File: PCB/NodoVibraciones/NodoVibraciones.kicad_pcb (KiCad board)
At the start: 2 copper layers, 62 x 33 mm, 26 parts, among them J1 batería, J2 UART, J4 MPU6050, SW2 SW_Push, U1 ESP-07, U2 module_mpu6050, U3 AMS1117-3.3

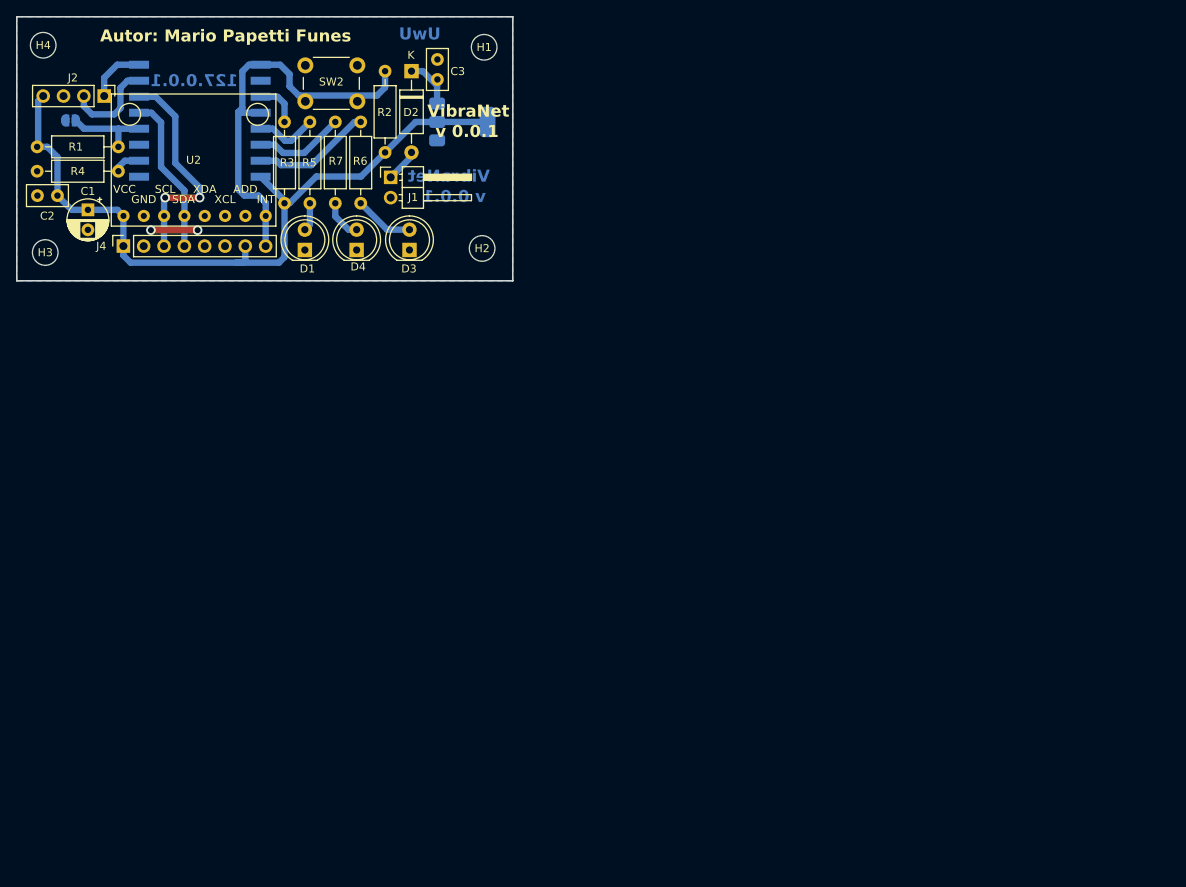
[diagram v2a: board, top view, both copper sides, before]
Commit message: Se implementaron interrupciones y diseño de PCB v1.0.8
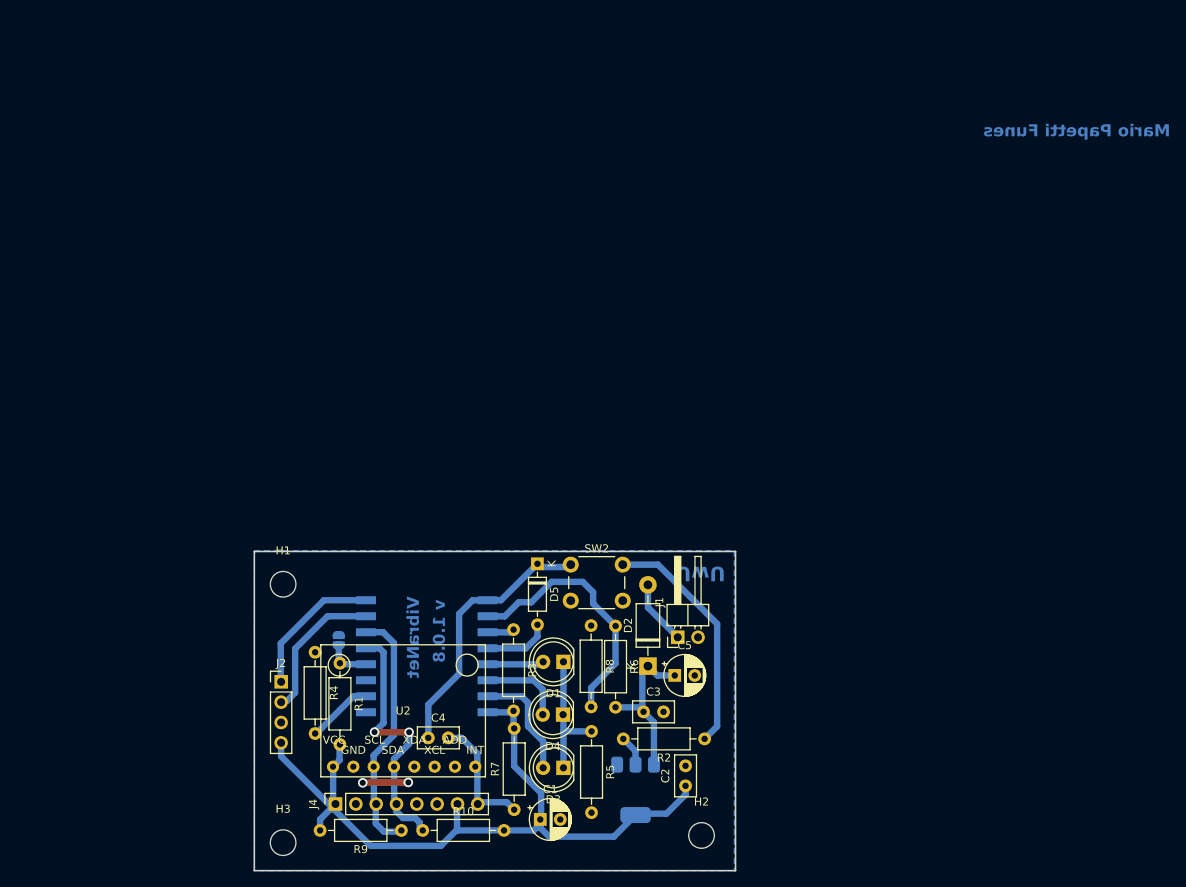
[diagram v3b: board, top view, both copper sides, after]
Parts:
- removed H4: MountingHole, MountingHole:MountingHole_3.2mm_M3
- added C4: 104, Capacitor_THT:C_Disc_D5.0mm_W2.5mm_P2.50mm, F.Cu at (74.8, 115.1)
- added C5: 10uf, Capacitor_THT:CP_Radial_D5.0mm_P2.50mm, F.Cu at (105.7, 107.3)
- added D5: 1N4148, Diode_THT:D_DO-35_SOD27_P7.62mm_Horizontal, F.Cu at (88.5, 93.3)
- added R10: 4k7, Resistor_THT:R_Axial_DIN0207_L6.3mm_D2.5mm_P10.16mm_Horizontal, F.Cu at (74.2, 126.7)
- added R8: 100k, Resistor_THT:R_Axial_DIN0207_L6.3mm_D2.5mm_P10.16mm_Horizontal, F.Cu at (95.2, 101.1)
- added R9: 4k7, Resistor_THT:R_Axial_DIN0207_L6.3mm_D2.5mm_P10.16mm_Horizontal, F.Cu at (71.5, 126.7)
- C1: value 47uF -> 10uf
- D2: value 1N4007 -> 1N5817; footprint Diode_THT:D_A-405_P10.16mm_Horizontal -> Diode_THT:D_DO-41_SOD81_P10.16mm_Horizontal
- JP1: value Jumper_2_Open -> Jumper_Boot
- R6: value 1k -> 330k
- R7: value 1k -> 10k
- moved C2 107.7 mm to (107.0, 121.1), turned to 90 degrees
- moved C1 94.9 mm to (88.8, 125.3), turned to 0 degrees
- moved R2 92.5 mm to (109.4, 115.2), turned to 180 degrees
- moved U3 86.2 mm to (100.8, 121.6), turned to -90 degrees
- moved C3 83.1 mm to (101.8, 111.8), turned to 0 degrees
- moved D2 80.0 mm to (102.3, 106.1), turned to 90 degrees
- moved H3 79.5 mm to (56.7, 128.2)
- moved R7 79.0 mm to (85.6, 124.1)
- moved H2 78.3 mm to (109.0, 127.3)
- moved J2 76.5 mm to (56.5, 108.1), turned to 0 degrees
- moved R5 74.8 mm to (95.2, 114.3), turned to -90 degrees
- moved J4 74.6 mm to (63.2, 123.4)
- moved U2 73.7 mm to (80.7, 118.7)
- moved JP1 73.1 mm to (63.6, 102.9), turned to -90 degrees
- moved U1 72.7 mm to (74.7, 102.8)
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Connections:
- C3 pad 1: /Vin -> Bat
- D1 pad 1: GNDREF -> Net-(D1-K)
- D1 pad 2: Net-(D1-A) -> /led-aux
- D2 pad 1: /Vin -> Bat
- D3 pad 1: GNDREF -> Net-(D1-K)
- D3 pad 2: Net-(D3-A) -> /led-data
- D4 pad 1: GNDREF -> Net-(D1-K)
- D4 pad 2: Net-(D4-A) -> /led-wifi
- R2 pad 1: int1 -> /reset
- R5 pad 1: Net-(D1-A) -> Net-(D1-K)
- R5 pad 2: /led-aux -> GNDREF
- R6 pad 1: Net-(D3-A) -> Net-(U1-ADC)
- R6 pad 2: /led-data -> Bat
- R7 pad 1: Net-(D4-A) -> int1
- R7 pad 2: /led-wifi -> VCC
- SW2 pad 1: int1 -> /reset
- U1 pad 1: int1 -> /reset
- U1 pad 2: unconnected-(U1-ADC-Pad2) -> Net-(U1-ADC)
- U1 pad 4: int1 -> Net-(D5-A)
- U3 pad 3: /Vin -> Bat
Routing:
- net /reset: track 0.00 -> 64.4 mm
- net int1: track 50.5 -> 15.7 mm
- net Net-(U1-ADC): track 0.00 -> 32.2 mm
- net Bat: track 0.00 -> 19.8 mm
- net Net-(D1-K): track 0.00 -> 16.8 mm
- net SDA: track 19.9 -> 32.4 mm, vias 0 -> 2
- net TX: track 7.32 -> 17.7 mm
- net VCC: track 93.5 -> 101.9 mm
- net Net-(D5-A): track 0.00 -> 8.24 mm
- net Net-(D3-A): track 7.46 -> 0.00 mm
- net RX: track 11.8 -> 18.3 mm
- net /Vin: track 6.20 -> 0.00 mm
- net Net-(D4-A): track 5.00 -> 0.00 mm
- net /magic: track 3.42 -> 8.34 mm
- net boot: track 10.6 -> 5.91 mm
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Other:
- board size 62 x 33 mm -> 60.1 x 39.9 mm
- board text added: "Mario Papetti Funes"
- board text added: "v 1.0.8"
- board text removed: "127.0.0.1"
- board text removed: "Autor: Mario Papetti Funes"
- board text removed: "v 0.0.1"

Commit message: Lanzamiento primer prototipo funcional ESP07 verHW1.5
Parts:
- added H4: MountingHole, MountingHole:MountingHole_3.2mm_M3, F.Cu at (3.48, 3.48)
- added R11: 10k, Resistor_THT:R_Axial_DIN0207_L6.3mm_D2.5mm_P7.62mm_Horizontal, F.Cu at (63.8, 108.3)
- C4: value 104 -> 10uF; footprint Capacitor_THT:C_Disc_D5.0mm_W2.5mm_P2.50mm -> Capacitor_THT:CP_Radial_D5.0mm_P2.50mm
- R1, R10, R2, R4, R5, R6, R7, R8, R9: footprint Resistor_THT:R_Axial_DIN0207_L6.3mm_D2.5mm_P10.16mm_Horizontal -> Resistor_THT:R_Axial_DIN0207_L6.3mm_D2.5mm_P7.62mm_Horizontal
- moved R4 19.1 mm to (59.9, 123.5), turned to 90 degrees
- moved D5 7.62 mm to (88.5, 101.0), turned to 90 degrees
- moved JP1 7.54 mm to (60.5, 109.8), turned to 90 degrees
- moved R1 3.30 mm to (60.5, 105.8)
- moved R2 2.57 mm to (106.8, 115.2)
- moved H2 1.00 mm to (109.6, 128.1)
- moved H1 0.61 mm to (56.8, 95.3)
- moved H3 0.14 mm to (56.8, 128.1)
- moved C4 0.11 mm to (74.8, 115.0)
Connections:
- D5 pad 1: /reset -> Net-(D5-K)
- D5 pad 2: Net-(D5-A) -> /reset
- U1 pad 11: unconnected-(U1-GPIO2-Pad11) -> Net-(U1-GPIO2)
- U1 pad 4: Net-(D5-A) -> Net-(D5-K)
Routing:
- net Net-(D5-K): track 0.00 -> 8.24 mm
- net Net-(D5-A): track 8.24 -> 0.00 mm
- net GNDREF: track 5.57 -> 12.9 mm, vias 2 -> 4
- net boot: track 5.91 -> 9.92 mm
- net VCC: track 101.9 -> 105.9 mm
- net Net-(U1-GPIO2): track 0.00 -> 3.42 mm
- net Net-(U1-ADC): track 32.2 -> 29.8 mm
- net /magic: track 8.34 -> 10.6 mm
- net Bat: track 19.8 -> 21.6 mm
- net /reset: track 64.4 -> 65.5 mm
- net TX: track 17.7 -> 16.7 mm
- net RX: track 18.3 -> 17.5 mm
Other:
- board text added: "v 1.1.2"
- board text removed: "v 1.0.8"
